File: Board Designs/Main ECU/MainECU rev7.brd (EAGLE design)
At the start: 120.6 x 78.9 mm, 196 parts, among them J1 JUMPER, J2 JUMPER, J3 JUMPER, J4 JUMPER, J5 JUMPER, J6 JUMPER, J7 JUMPER, J8 JUMPER, P1 SOLDER_PAD, P2 SOLDER_PAD, Q1 P-CHANNEL_MOSFET_DMP3099L-7, Q12 P-CHANNEL_MOSFET_DMP3099L-7, X1 CONNECTOR-37, X2 CONNECTOR-4AUTOSPORT, X3 CONNECTOR-4NANO-FIT-VERTICAL-4, X4 CONNECTOR-4NANO-FIT-VERTICAL-4

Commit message: Moved changes to new rev 7 for main ECU
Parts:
- added C27, C28, C29, R64, R65, R66: (no value), HyTechDevices:0805
- U$4, U$6, U$7: value N-CHANNEL_MOSFET_FQP30N06L -> N-CHANNEL_MOSFET_IRF1324PBF
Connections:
- new net N$65: C27.1, R64.1
- new net N$74: C28.1, R65.1
- new net N$75: C29.1, R66.1
- net CURRENTSENSE2: now also R64.2, R65.2, R66.2
- net FAN1-: now also C28.2
- net FAN2-: now also C27.2
- net PUMP1-: now also C29.2
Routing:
- net CURRENTSENSE2: track 43.6 -> 79.6 mm, vias 0 -> 1
- net FAN2-: track 10.6 -> 25.1 mm
- net N$6: track 43.3 -> 51.1 mm
- net PUMP1-: track 3.78 -> 9.14 mm
- net FAN1-: track 9.51 -> 13.5 mm
- net N$74: track 0.00 -> 2.19 mm
- net N$75: track 0.00 -> 1.78 mm
- net N$65: track 0.00 -> 1.74 mm

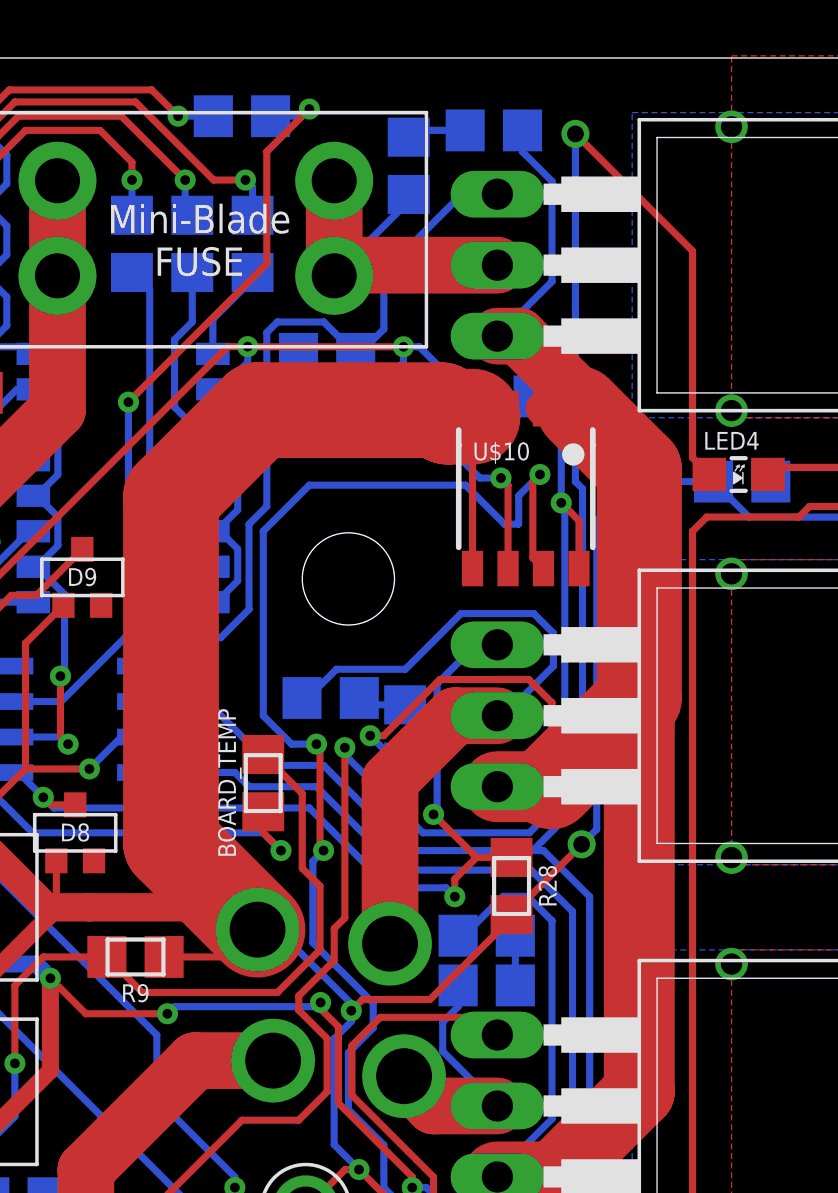
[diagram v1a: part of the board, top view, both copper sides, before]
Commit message: Flipped Resistor and capacitor posistions
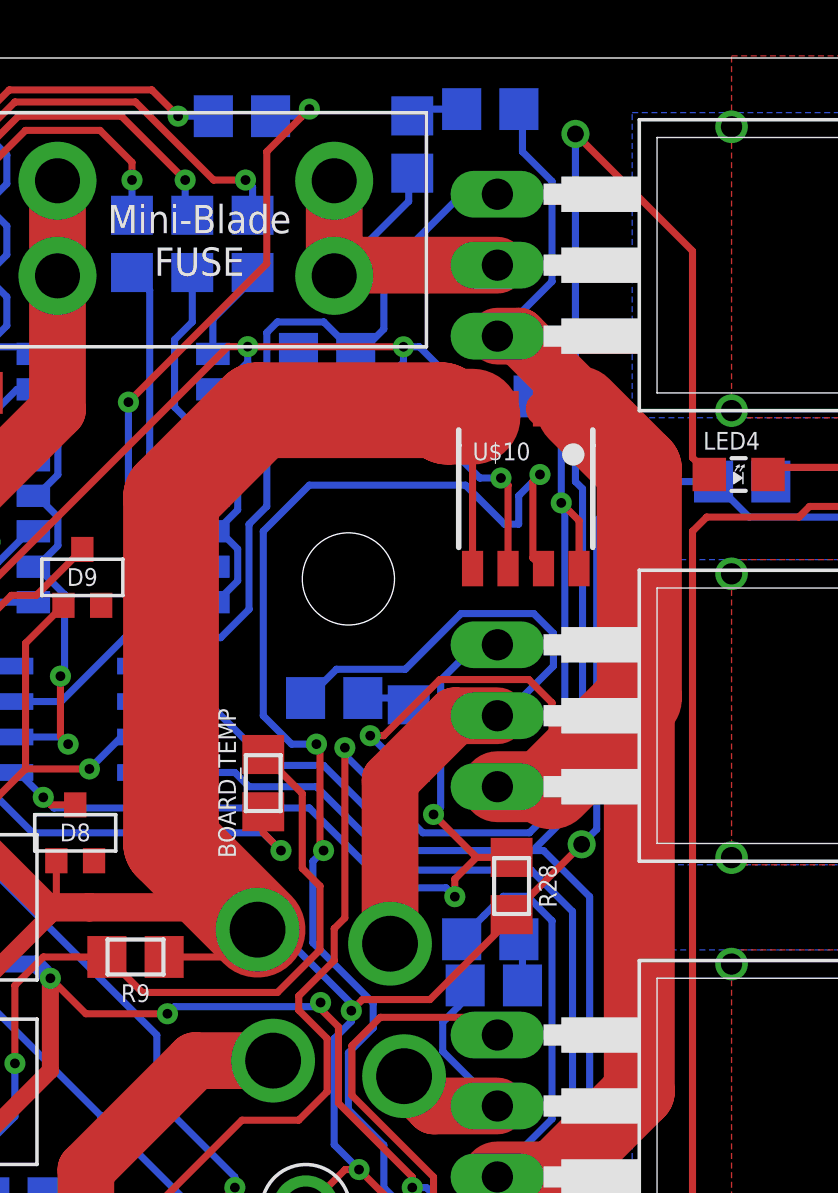
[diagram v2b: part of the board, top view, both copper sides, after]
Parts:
- moved C28 3.56 mm to (99.3, 77.1), turned to 180 degrees
- moved C27 3.07 mm to (96.4, 54.7), turned to 270 degrees
- moved R65 2.96 mm to (96.5, 75.8), turned to 90 degrees
- moved R64 2.84 mm to (93.7, 56.0), turned to 180 degrees
- moved R66 1.80 mm to (99.4, 45.7), turned to 180 degrees
- moved C29 1.66 mm to (99.3, 47.4)
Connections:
- net CURRENTSENSE2: now also C27.2, C28.2, C29.2; no longer R64.2, R65.2, R66.2
- net FAN1-: now also R65.1; no longer C28.2
- net FAN2-: now also R64.1; no longer C27.2
- net N$65: now also R64.2; no longer R64.1
- net N$74: now also R65.2; no longer R65.1
- net N$75: now also R66.2; no longer R66.1
- net PUMP1-: now also R66.1; no longer C29.2
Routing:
- net CURRENTSENSE2: track 79.6 -> 80.5 mm
- net FAN1-: track 13.5 -> 14.3 mm

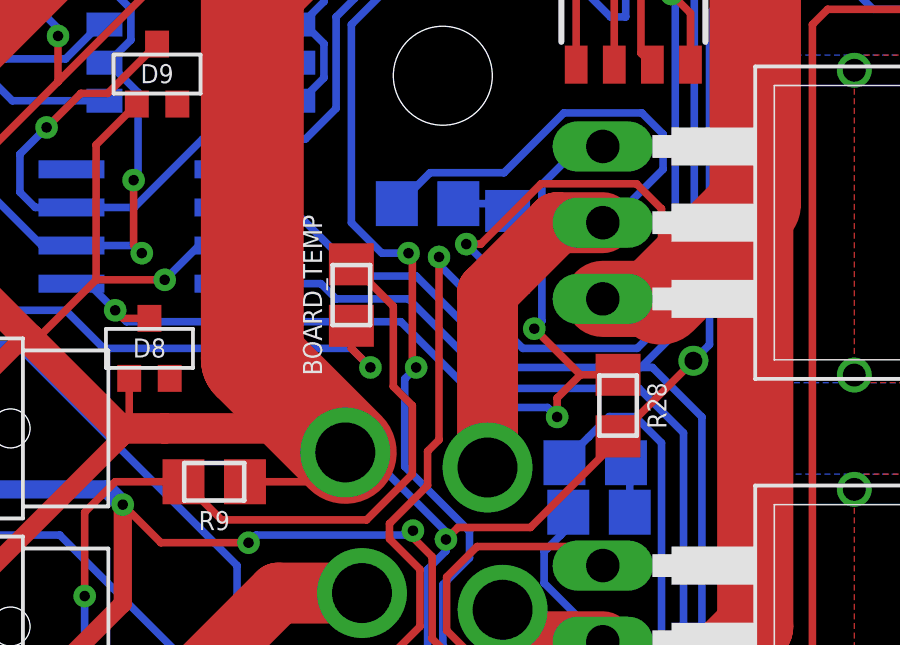
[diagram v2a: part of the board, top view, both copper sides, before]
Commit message: Added silkscreen for snubber parts
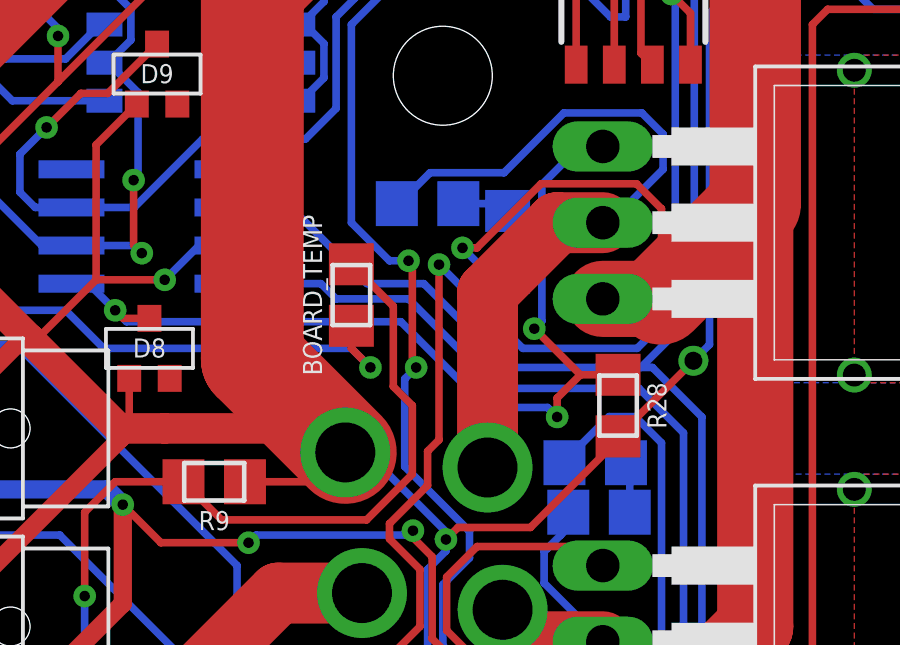
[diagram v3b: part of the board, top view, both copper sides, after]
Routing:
- net TELEMETRY5V: track 321.3 -> 320.8 mm
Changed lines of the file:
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@@
 </element>
 <element name="R64" library="HyTechDevices" package="0805" value="" x="93.726" y="56.007" smashed="yes" rot="MR180">
-<attribute name="NAME" x="93.726" y="55.2831" size="0.3048" layer="26" rot="MR180" align="bottom-center"/>
+<attribute name="NAME" x="93.726" y="55.1561" size="0.635" layer="26" rot="MR180" align="bottom-center"/>
 <attribute name="VALUE" x="93.726" y="56.7182" size="0.3048" layer="28" rot="MR180" align="top-center"/>
 </element>
 <element name="C27" library="HyTechDevices" package="0805" value="" x="96.393" y="54.737" smashed="yes" rot="MR270">
-<attribute name="NAME" x="95.6691" y="54.737" size="0.3048" layer="26" rot="MR270" align="bottom-center"/>
+<attribute name="NAME" x="97.8281" y="54.737" size="0.635" layer="26" rot="MR270" align="bottom-center"/>
 <attribute name="VALUE" x="97.1042" y="54.737" size="0.3048" layer="28" rot="MR270" align="top-center"/>
 </element>
 <element name="R65" library="HyTechDevices" package="0805" value="" x="96.52" y="75.819" smashed="yes" rot="MR90">
-<attribute name="NAME" x="97.2439" y="75.819" size="0.3048" layer="26" rot="MR90" align="bottom-center"/>
+<attribute name="NAME" x="97.3709" y="75.438" size="0.635" layer="26" rot="MR90" align="bottom-center"/>
 <attribute name="VALUE" x="95.8088" y="75.819" size="0.3048" layer="28" rot="MR90" align="top-center"/>
 </element>
 <element name="C28" library="HyTechDevices" package="0805" value="" x="99.314" y="77.089" smashed="yes" rot="MR180">
-<attribute name="NAME" x="99.314" y="76.3651" size="0.3048" layer="26" rot="MR180" align="bottom-center"/>
+<attribute name="NAME" x="99.314" y="76.2381" size="0.635" layer="26" rot="MR180" align="bottom-center"/>
 <attribute name="VALUE" x="99.314" y="77.8002" size="0.3048" layer="28" rot="MR180" align="top-center"/>
 </element>
 <element name="R66" library="HyTechDevices" package="0805" value="" x="99.441" y="45.72" smashed="yes" rot="MR180">
-<attribute name="NAME" x="99.441" y="44.9961" size="0.3048" layer="26" rot="MR180" align="bottom-center"/>
+<attribute name="NAME" x="97.6249" y="45.72" size="0.635" layer="26" rot="MR270" align="bottom-center"/>
 <attribute name="VALUE" x="99.441" y="46.4312" size="0.3048" layer="28" rot="MR180" align="top-center"/>
 </element>
 <element name="C29" library="HyTechDevices" package="0805" value="" x="99.314" y="47.371" smashed="yes" rot="MR0">
-<attribute name="NAME" x="99.314" y="48.0949" size="0.3048" layer="26" rot="MR0" align="bottom-center"/>
+<attribute name="NAME" x="99.314" y="48.2219" size="0.635" layer="26" rot="MR0" align="bottom-center"/>
 <attribute name="VALUE" x="99.314" y="46.6598" size="0.3048" layer="28" rot="MR0" align="top-center"/>
 </element>
@@
 <wire x1="101.5238" y1="48.03133125" x2="100.64673125" y2="48.9084" width="0.254" layer="16"/>
 <wire x1="101.5238" y1="40.93906875" x2="101.5238" y2="48.03133125" width="0.254" layer="16"/>
-<wire x1="99.77726875" y1="48.9084" x2="99.094434375" y2="48.225565625" width="0.254" layer="16"/>
-<via x="95.0158" y="54.658034375" extent="1-16" drill="0.35"/>
-<wire x1="99.094434375" y1="48.225565625" x2="98.36686875" y2="47.498" width="0.254" layer="16"/>
+<via x="94.8888" y="54.531034375" extent="1-16" drill="0.35"/>
+<wire x1="99.77726875" y1="48.9084" x2="98.289" y2="47.42013125" width="0.254" layer="16"/>
 <wire x1="97.507425" y1="56.6674" x2="100.69133125" y2="56.6674" width="0.254" layer="1"/>
 <wire x1="100.69133125" y1="56.6674" x2="101.5238" y2="55.83493125" width="0.254" layer="1"/>
-<wire x1="95.961834375" y1="53.712" x2="95.0158" y2="54.658034375" width="0.254" layer="16"/>
-<wire x1="95.0158" y1="54.658034375" x2="95.498059375" y2="54.658034375" width="0.254" layer="1"/>
-<wire x1="95.498059375" y1="54.658034375" x2="97.507425" y2="56.6674" width="0.254" layer="1"/>
+<wire x1="95.707834375" y1="53.712" x2="94.8888" y2="54.531034375" width="0.254" layer="16"/>
+<wire x1="94.8888" y1="54.531034375" x2="95.371059375" y2="54.531034375" width="0.254" layer="1"/>
+<wire x1="95.371059375" y1="54.531034375" x2="97.507425" y2="56.6674" width="0.254" layer="1"/>
 <contactref element="C28" pad="2"/>
 <contactref element="C27" pad="2"/>
@@
 <wire x1="101.5238" y1="55.83493125" x2="101.5238" y2="54.7878" width="0.254" layer="1"/>
 <wire x1="101.5238" y1="54.7878" x2="99.568" y2="52.832" width="0.254" layer="1"/>
-<wire x1="96.393" y1="53.712" x2="95.961834375" y2="53.712" width="0.254" layer="16"/>
+<wire x1="96.393" y1="53.712" x2="95.707834375" y2="53.712" width="0.254" layer="16"/>
 <wire x1="98.289" y1="47.371" x2="98.289" y2="47.42013125" width="0.254" layer="16"/>
-<wire x1="98.289" y1="47.42013125" x2="98.36686875" y2="47.498" width="0.254" layer="16"/>
 </signal>
 <signal name="SHUTDOWN_C">
@@
 <wire x1="95.123" y1="45.085" x2="95.123" y2="44.196" width="0.254" layer="16"/>
 <via x="93.345" y="50.546" extent="1-16" drill="0.35"/>
-<wire x1="93.091" y1="54.356" x2="93.218" y2="54.229" width="0.254" layer="1"/>
-<wire x1="93.218" y1="54.229" x2="93.218" y2="50.673" width="0.254" layer="1"/>
+<wire x1="93.218" y1="53.975" x2="93.091" y2="54.102" width="0.254" layer="1"/>
+<wire x1="93.218" y1="53.975" x2="93.218" y2="50.673" width="0.254" layer="1"/>
 <wire x1="93.218" y1="50.673" x2="93.345" y2="50.546" width="0.254" layer="1"/>
-<via x="93.091" y="54.356" extent="1-16" drill="0.35"/>
+<via x="93.091" y="54.102" extent="1-16" drill="0.35"/>
 <wire x1="93.345" y1="50.546" x2="92.964" y2="50.165" width="0.254" layer="16"/>
 <wire x1="92.964" y1="50.165" x2="92.964" y2="47.244" width="0.254" layer="16"/>
 <wire x1="91.186" y1="61.976" x2="91.186" y2="55.372" width="0.254" layer="16"/>
-<wire x1="92.202" y1="54.356" x2="93.091" y2="54.356" width="0.254" layer="16"/>
-<wire x1="92.202" y1="54.356" x2="91.186" y2="55.372" width="0.254" layer="16"/>
+<wire x1="92.456" y1="54.102" x2="93.091" y2="54.102" width="0.254" layer="16"/>
+<wire x1="92.456" y1="54.102" x2="91.186" y2="55.372" width="0.254" layer="16"/>
 <wire x1="98.425" y1="63.627" x2="92.837" y2="63.627" width="0.254" layer="16"/>
 <wire x1="92.837" y1="63.627" x2="91.186" y2="61.976" width="0.254" layer="16"/>
@@
 <wire x1="92.456" y1="44.831" x2="93.472" y2="43.815" width="0.254" layer="1"/>
 <wire x1="93.472" y1="43.815" x2="93.472" y2="41.91" width="0.254" layer="1"/>
-<via x="94.107" y="54.229" extent="1-16" drill="0.35"/>
-<wire x1="94.107" y1="54.229" x2="94.107" y2="48.133" width="0.254" layer="1"/>
+<via x="94.107" y="53.975" extent="1-16" drill="0.35"/>
+<wire x1="94.107" y1="53.975" x2="94.107" y2="48.133" width="0.254" layer="1"/>
 <wire x1="115.824" y1="5.334" x2="95.631" y2="5.334" width="0.254" layer="1"/>
 <wire x1="95.631" y1="5.334" x2="75.2412" y2="5.334" width="0.254" layer="1"/>
@@
 <wire x1="100.711" y1="51.181" x2="96.901" y2="51.181" width="0.254" layer="16"/>
 <wire x1="96.901" y1="51.181" x2="94.107" y2="53.975" width="0.254" layer="16"/>
-<wire x1="94.107" y1="54.229" x2="94.107" y2="53.975" width="0.254" layer="16"/>
 <wire x1="54.61" y1="27.559" x2="53.7845" y2="26.7335" width="0.254" layer="1"/>
 <wire x1="101.854" y1="62.992" x2="101.981" y2="62.865" width="0.254" layer="16"/>
@@
 <contactref element="U$5" pad="2"/>
 <wire x1="102.87" y1="48.895" x2="102.87" y2="36.322" width="0.254" layer="16"/>
-<wire x1="93.345" y1="53.594" x2="96.393" y2="50.546" width="0.254" layer="16"/>
+<wire x1="93.599" y1="53.34" x2="96.393" y2="50.546" width="0.254" layer="16"/>
 <wire x1="101.219" y1="50.546" x2="102.87" y2="48.895" width="0.254" layer="16"/>
 <wire x1="96.393" y1="50.546" x2="100.838" y2="50.546" width="0.254" layer="16"/>
 <wire x1="100.838" y1="50.546" x2="101.219" y2="50.546" width="0.254" layer="16"/>
-<wire x1="91.4552375" y1="53.594" x2="93.345" y2="53.594" width="0.254" layer="16"/>
+<wire x1="91.7092375" y1="53.34" x2="93.599" y2="53.34" width="0.254" layer="16"/>
 <wire x1="46.3042" y1="9.8806" x2="48.26" y2="11.8364" width="0.254" layer="16"/>
 <wire x1="55.9816" y1="11.8364" x2="57.912" y2="9.906" width="0.254" layer="16"/>
@@
 <wire x1="101.092" y1="6.096" x2="77.089" y2="6.096" width="0.254" layer="1"/>
 <wire x1="87.055" y1="55.88" x2="89.1692375" y2="55.88" width="0.254" layer="16"/>
-<wire x1="89.1692375" y1="55.88" x2="91.4552375" y2="53.594" width="0.254" layer="16"/>
+<wire x1="89.1692375" y1="55.88" x2="91.7092375" y2="53.34" width="0.254" layer="16"/>
 <contactref element="LED4" pad="A"/>
 <wire x1="107.154" y1="64.008" x2="106.553" y2="64.609" width="0.254" layer="1"/>

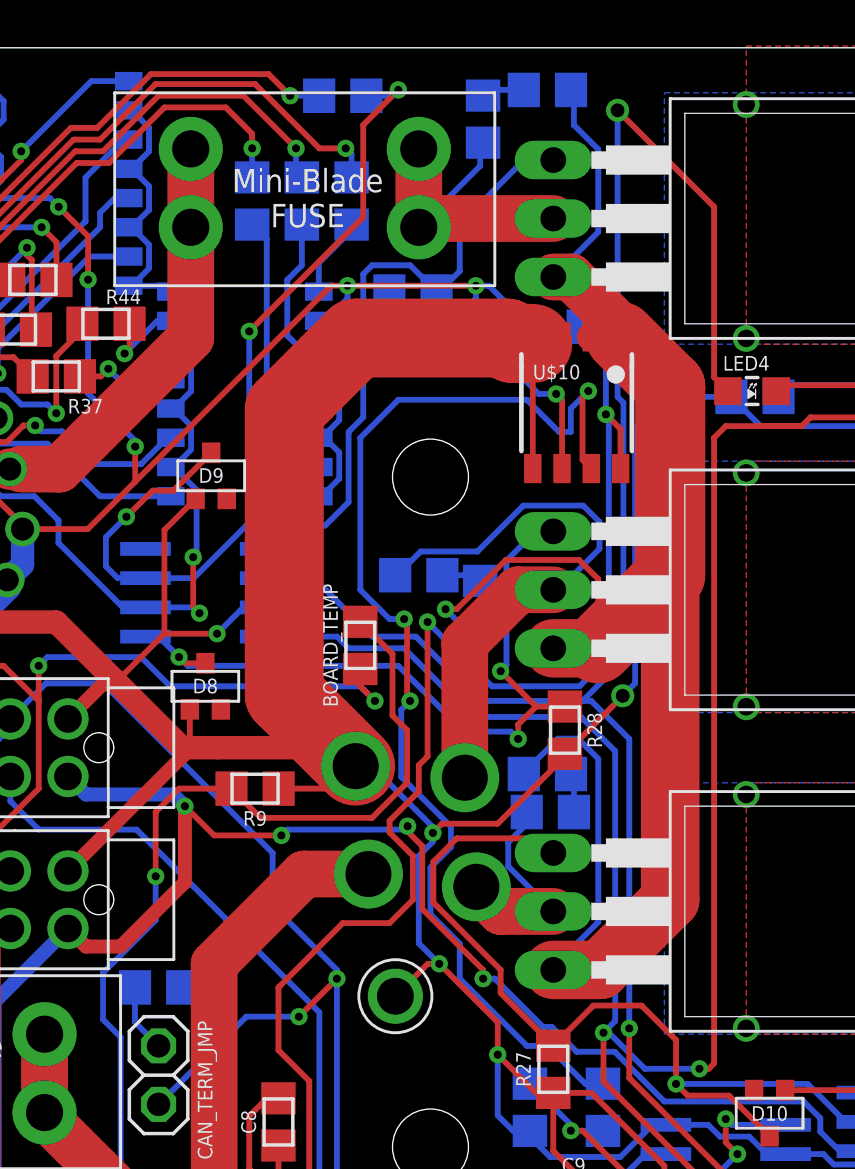
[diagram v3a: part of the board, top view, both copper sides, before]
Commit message: Tweaks to RC snubber components and traces
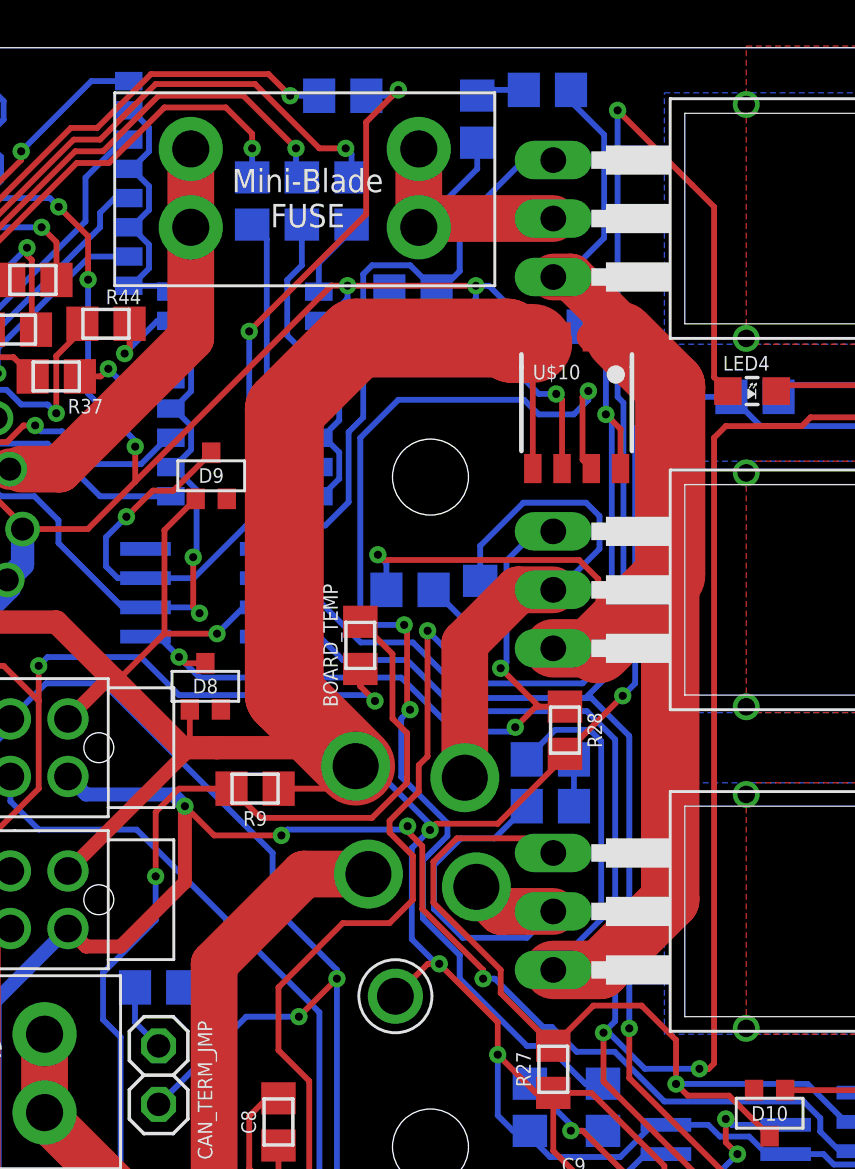
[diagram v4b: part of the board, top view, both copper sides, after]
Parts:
- moved C27 3.11 mm to (93.3, 55.4), turned to 0 degrees
- moved R64 2.95 mm to (96.4, 54.7), turned to 270 degrees
- moved C29 0.65 mm to (99.4, 48.0)
- moved R66 0.25 mm to (99.4, 46.0)
- moved R65 0.25 mm to (96.3, 75.8)
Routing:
- net PUMP1-: track 9.24 -> 17.0 mm
- net CURRENTSENSE2: track 80.8 -> 83.8 mm
- net FAN2-: track 25.0 -> 22.5 mm
- net N$65: track 1.74 -> 2.71 mm
- net FAN2DRIVE: track 31.9 -> 31.3 mm
- net TELEMETRY5V: track 320.8 -> 320.2 mm
